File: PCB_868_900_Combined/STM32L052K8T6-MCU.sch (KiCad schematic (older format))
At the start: 27 parts, among them J2 20021121-00010C4LF, J3 B4B-PH-K-S(LF)(SN), J5 0475890001-MicroUSBPort, P1 CONN_02X03, SW2 B3U-1000P, U3 STM32L052C8T6, X3 ABM10-166-12.000MHZ-T3

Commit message: Change and Progress
connecotrs change to SMA, implemented combined PA/LNA match, currently
working on that version as primary. PCB components are placed and board
size is almost set.
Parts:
- removed J3: B4B-PH-K-S(LF)(SN), PCB_Footprints:B4B-PH-K-S(LF)(SN), symbol B4B-PH-K-S(LF)(SN)
- removed P1: CONN_02X03, Pin_Headers:Pin_Header_Straight_2x03, symbol CONN_02X03
- added J3, J4: SM06B-SRSS-TB(LF)(SN), PCB_Footprints:SM06B-SRSS-TB(LF)(SN), symbol SM06B-SRSS-TB(LF)(SN)
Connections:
- wire segments 74 -> 93

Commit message: RF Shield and more progress
Adding an RF shield to the combined implementation of the 915MHZ version
of S1G. Also experimenting with differnt connectors and what not.
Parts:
- removed J3, J4: SM06B-SRSS-TB(LF)(SN), PCB_Footprints:SM06B-SRSS-TB(LF)(SN), symbol SM06B-SRSS-TB(LF)(SN)
- added P1: CONN_02X08, Pin_Headers:Pin_Header_Straight_2x08, symbol CONN_02X08
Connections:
- net labels added: PSU_IN, VIN
- wire segments 93 -> 76

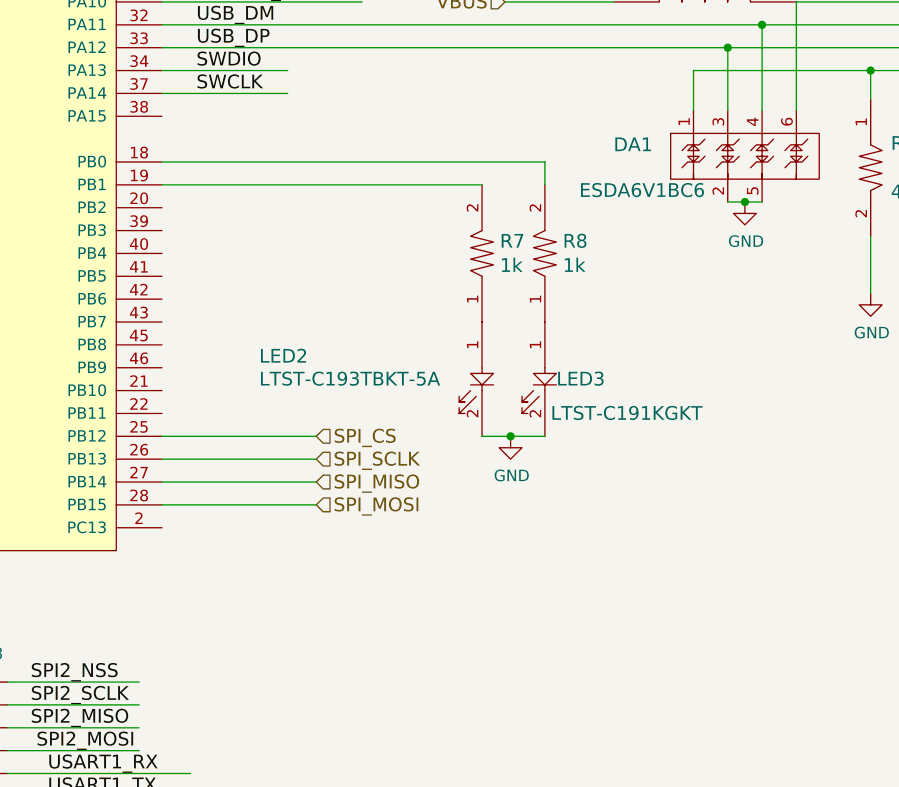
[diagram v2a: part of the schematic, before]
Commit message: First pass on PCB
First pass on PCB completed. PCB_868_900_Combined is the folder for the
finished rev.
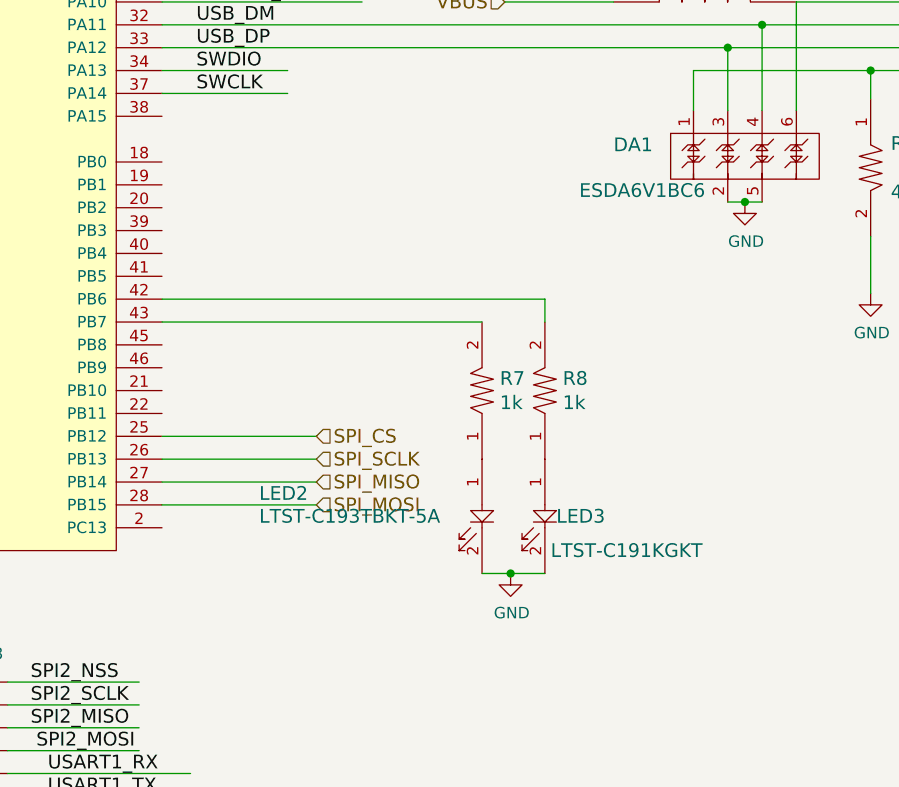
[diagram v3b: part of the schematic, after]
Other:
- moved on the sheet: LED2, LED3, R7, R8

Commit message: PCBs Tweaked A lot
PCBs have been tweaked. The separate implementation has been finished
but also has GPIOs from the MCU broken out to the connector, same for
the combined implementation. Both boards now have power indication LEDs
(red).
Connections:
- net labels added: GPIO_PA8, GPIO_PB0, GPIO_PB1, GPIO_PB10, GPIO_PB11, GPIO_PB2
- wire segments 76 -> 88
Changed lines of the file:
@@
 F 3 "" H 5575 5625 50  0000 C CNN
 	1    5575 6825
-	1    0    0    -1
+	-1   0    0    1
 $EndComp
 Text Label 6000 6975 0    60   ~ 0
 USART1_TX
-Text Label 6000 6875 0    60   ~ 0
+Text Label 4825 6975 0    60   ~ 0
 USART1_RX
 Wire Wire Line
 	5825 6975 6625 6975
 Wire Wire Line
-	5825 6875 6625 6875
-Text Label 5950 6775 0    60   ~ 0
+	4525 6975 5325 6975
+Text Label 4825 6575 0    60   ~ 0
 SPI2_MOSI
-Text Label 5925 6675 0    60   ~ 0
+Text Label 5925 6575 0    60   ~ 0
 SPI2_MISO
-Text Label 5925 6575 0    60   ~ 0
+Text Label 4825 6475 0    60   ~ 0
 SPI2_SCLK
 Text Label 5925 6475 0    60   ~ 0
 SPI2_NSS
 Wire Wire Line
-	6400 6775 5825 6775
+	5325 6575 4750 6575
 Wire Wire Line
-	5825 6575 6400 6575
+	4750 6475 5325 6475
 Wire Wire Line
 	5825 6475 6400 6475
 Wire Wire Line
-	5825 6675 6400 6675
+	5825 6575 6400 6575
 Text HLabel 10975 5250 2    60   Input ~ 0
 VIN
@@
 Text Label 10300 5250 0    60   ~ 0
 PSU_IN
-Text Label 5950 7075 0    60   ~ 0
+Text Label 4875 7175 0    60   ~ 0
 PSU_IN
 Wire Wire Line
-	6400 7075 5825 7075
+	5325 7175 4750 7175
 $Comp
 L GND #PWR42
@@
 L GND #PWR41
 U 1 1 5824B1D0
-P 5325 7175
-F 0 "#PWR41" H 5325 6925 50  0001 C CNN
-F 1 "GND" H 5330 7002 50  0000 C CNN
-F 2 "" H 5325 7175 50  0000 C CNN
-F 3 "" H 5325 7175 50  0000 C CNN
-	1    5325 7175
+P 4350 7175
+F 0 "#PWR41" H 4350 6925 50  0001 C CNN
+F 1 "GND" H 4355 7002 50  0000 C CNN
+F 2 "" H 4350 7175 50  0000 C CNN
+F 3 "" H 4350 7175 50  0000 C CNN
+	1    4350 7175
 	1    0    0    -1
 $EndComp
+Text Label 6500 4200 0    60   ~ 0
+GPIO_PB0
+Text Label 6500 4300 0    60   ~ 0
+GPIO_PB1
+Text Label 6500 4400 0    60   ~ 0
+GPIO_PB2
+Text Label 6500 5200 0    60   ~ 0
+GPIO_PB10
+Text Label 6500 5300 0    60   ~ 0
+GPIO_PB11
+Text Label 6675 3300 0    60   ~ 0
+GPIO_PA8
+Wire Wire Line
+	7225 3300 6500 3300
+Wire Wire Line
+	7050 4200 6500 4200
+Wire Wire Line
+	7050 4300 6500 4300
+Wire Wire Line
+	7050 4400 6500 4400
+Wire Wire Line
+	7050 5200 6500 5200
+Wire Wire Line
+	7050 5300 6500 5300
+Text Label 5925 6675 0    60   ~ 0
+GPIO_PB0
+Text Label 4825 6675 0    60   ~ 0
+GPIO_PB1
+Text Label 5825 6775 0    60   ~ 0
+GPIO_PB2
+Wire Wire Line
+	6375 6675 5825 6675
+Wire Wire Line
+	5325 6675 4775 6675
+Wire Wire Line
+	6375 6775 5825 6775
+Text Label 4825 6775 0    60   ~ 0
+GPIO_PB10
+Text Label 5825 6875 0    60   ~ 0
+GPIO_PB11
+Wire Wire Line
+	5325 6775 4775 6775
+Wire Wire Line
+	6375 6875 5825 6875
+Text Label 4825 6875 0    60   ~ 0
+GPIO_PA8
+Wire Wire Line
+	5325 6875 4600 6875
 $EndSCHEMATC

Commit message: Additional GPIO
Two additional GPIO pins from the STM32L0 have been added to the
connector, now there is a signal on every pin. The connector component
has been replaced with one that has a STEP 3D model for proper 3D model
exporting from KiCAD for enclosure design. This has been done to both
versions of the radio.
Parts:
- removed P1: CONN_02X08, Pin_Headers:Pin_Header_Straight_2x08, symbol CONN_02X08
- added P1: 61301621121, PCB_Footprints:61301621121, symbol 61301621121
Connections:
- net labels added: GPIO_PA15, GPIO_PB3
- wire segments 88 -> 92
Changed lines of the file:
@@
 $EndComp
 $Comp
-L GND #PWR31
+L GND #PWR030
 U 1 1 582190B8
 P 1400 5050
-F 0 "#PWR31" H 1400 4800 50  0001 C CNN
+F 0 "#PWR030" H 1400 4800 50  0001 C CNN
 F 1 "GND" H 1405 4877 50  0000 C CNN
 F 2 "" H 1400 5050 50  0000 C CNN
@@
 $EndComp
 $Comp
-L GND #PWR42
+L GND #PWR031
 U 1 1 58219186
 P 4750 5800
-F 0 "#PWR42" H 4750 5550 50  0001 C CNN
+F 0 "#PWR031" H 4750 5550 50  0001 C CNN
 F 1 "GND" H 4755 5627 50  0000 C CNN
 F 2 "" H 4750 5800 50  0000 C CNN
@@
 $EndComp
 $Comp
-L +3.3V #PWR30
+L +3.3V #PWR032
 U 1 1 58219330
 P 1400 4000
-F 0 "#PWR30" H 1400 3850 50  0001 C CNN
+F 0 "#PWR032" H 1400 3850 50  0001 C CNN
 F 1 "+3.3V" H 1415 4173 50  0000 C CNN
 F 2 "" H 1400 4000 50  0000 C CNN
@@
 $EndComp
 $Comp
-L GND #PWR39
+L GND #PWR033
 U 1 1 58219BE3
 P 3450 2950
-F 0 "#PWR39" H 3450 2700 50  0001 C CNN
+F 0 "#PWR033" H 3450 2700 50  0001 C CNN
 F 1 "GND" H 3455 2777 50  0000 C CNN
 F 2 "" H 3450 2950 50  0000 C CNN
@@
 $EndComp
 $Comp
-L +3.3V #PWR37
+L +3.3V #PWR034
 U 1 1 58219CF5
 P 3100 2500
-F 0 "#PWR37" H 3100 2350 50  0001 C CNN
+F 0 "#PWR034" H 3100 2350 50  0001 C CNN
 F 1 "+3.3V" H 3115 2673 50  0000 C CNN
 F 2 "" H 3100 2500 50  0000 C CNN
@@
 $EndComp
 $Comp
-L GND #PWR35
+L GND #PWR035
 U 1 1 5821A196
 P 1700 2950
-F 0 "#PWR35" H 1700 2700 50  0001 C CNN
+F 0 "#PWR035" H 1700 2700 50  0001 C CNN
 F 1 "GND" H 1705 2777 50  0000 C CNN
 F 2 "" H 1700 2950 50  0000 C CNN
@@
 $EndComp
 $Comp
-L GND #PWR36
+L GND #PWR036
 U 1 1 5821A1E0
 P 2500 2950
-F 0 "#PWR36" H 2500 2700 50  0001 C CNN
+F 0 "#PWR036" H 2500 2700 50  0001 C CNN
 F 1 "GND" H 2505 2777 50  0000 C CNN
 F 2 "" H 2500 2950 50  0000 C CNN
@@
 $EndComp
 $Comp
-L +3.3V #PWR34
+L +3.3V #PWR037
 U 1 1 5821A692
 P 1500 2500
-F 0 "#PWR34" H 1500 2350 50  0001 C CNN
+F 0 "#PWR037" H 1500 2350 50  0001 C CNN
 F 1 "+3.3V" H 1515 2673 50  0000 C CNN
 F 2 "" H 1500 2500 50  0000 C CNN
@@
 $EndComp
 $Comp
-L GND #PWR47
+L GND #PWR038
 U 1 1 58221381
 P 9975 3900
-F 0 "#PWR47" H 9975 3650 50  0001 C CNN
+F 0 "#PWR038" H 9975 3650 50  0001 C CNN
 F 1 "GND" H 9980 3727 50  0000 C CNN
 F 2 "" H 9975 3900 50  0000 C CNN
@@
 $EndComp
 $Comp
-L GND #PWR49
+L GND #PWR039
 U 1 1 58221B76
 P 10475 4775
-F 0 "#PWR49" H 10475 4525 50  0001 C CNN
+F 0 "#PWR039" H 10475 4525 50  0001 C CNN
 F 1 "GND" H 10480 4602 50  0000 C CNN
 F 2 "" H 10475 4775 50  0000 C CNN
@@
 $EndComp
 $Comp
-L GND #PWR46
+L GND #PWR040
 U 1 1 58223B2D
 P 9600 4775
-F 0 "#PWR46" H 9600 4525 50  0001 C CNN
+F 0 "#PWR040" H 9600 4525 50  0001 C CNN
 F 1 "GND" H 9605 4602 50  0000 C CNN
 F 2 "" H 9600 4775 50  0000 C CNN
@@
 $EndComp
 $Comp
-L GND #PWR45
+L GND #PWR041
 U 1 1 58224185
 P 9050 4375
-F 0 "#PWR45" H 9050 4125 50  0001 C CNN
+F 0 "#PWR041" H 9050 4125 50  0001 C CNN
 F 1 "GND" H 9055 4202 50  0000 C CNN
 F 2 "" H 9050 4375 50  0000 C CNN
@@
 $EndComp
 $Comp
-L GND #PWR48
+L GND #PWR042
 U 1 1 58224D2B
 P 10425 3125
-F 0 "#PWR48" H 10425 2875 50  0001 C CNN
+F 0 "#PWR042" H 10425 2875 50  0001 C CNN
 F 1 "GND" H 10430 2952 50  0000 C CNN
 F 2 "" H 10425 3125 50  0000 C CNN
@@
 NRST
 $Comp
-L GND #PWR33
+L GND #PWR043
 U 1 1 5824BA14
 P 1400 6250
-F 0 "#PWR33" H 1400 6000 50  0001 C CNN
+F 0 "#PWR043" H 1400 6000 50  0001 C CNN
 F 1 "GND" H 1405 6077 50  0000 C CNN
 F 2 "" H 1400 6250 50  0000 C CNN
@@
 $EndComp
 $Comp
-L +3.3V #PWR32
+L +3.3V #PWR044
 U 1 1 5824BBC1
 P 1400 5575
-F 0 "#PWR32" H 1400 5425 50  0001 C CNN
+F 0 "#PWR044" H 1400 5425 50  0001 C CNN
 F 1 "+3.3V" H 1415 5748 50  0000 C CNN
 F 2 "" H 1400 5575 50  0000 C CNN
@@
 $EndComp
 $Comp
-L GND #PWR44
+L GND #PWR045
 U 1 1 58250111
 P 8025 6000
-F 0 "#PWR44" H 8025 5750 50  0001 C CNN
+F 0 "#PWR045" H 8025 5750 50  0001 C CNN
 F 1 "GND" H 8030 5827 50  0000 C CNN
 F 2 "" H 8025 6000 50  0000 C CNN
@@
 $EndComp
 $Comp
-L GND #PWR40
+L GND #PWR046
 U 1 1 582650D6
 P 4150 4375
-F 0 "#PWR40" H 4150 4125 50  0001 C CNN
+F 0 "#PWR046" H 4150 4125 50  0001 C CNN
 F 1 "GND" H 4155 4202 50  0000 C CNN
 F 2 "" H 4150 4375 50  0000 C CNN
@@
 Connection ~ 3250 4200
 $Comp
-L GND #PWR38
+L GND #PWR047
 U 1 1 58299A73
 P 3125 4200
-F 0 "#PWR38" H 3125 3950 50  0001 C CNN
+F 0 "#PWR047" H 3125 3950 50  0001 C CNN
 F 1 "GND" H 3130 4027 50  0000 C CNN
 F 2 "" H 3125 4200 50  0000 C CNN
@@
 $EndComp
 Connection ~ 3125 4200
-$Comp
-L CONN_02X08 P1
-U 1 1 5823F6D4
-P 5575 6825
-F 0 "P1" H 5575 7390 50  0000 C CNN
-F 1 "CONN_02X08" H 5575 7299 50  0000 C CNN
-F 2 "Pin_Headers:Pin_Header_Straight_2x08" H 5575 5625 50  0001 C CNN
-F 3 "" H 5575 5625 50  0000 C CNN
-	1    5575 6825
-	-1   0    0    1
-$EndComp
-Text Label 6000 6975 0    60   ~ 0
+Text Label 6100 6975 0    60   ~ 0
 USART1_TX
 Text Label 4825 6975 0    60   ~ 0
 USART1_RX
 Wire Wire Line
-	5825 6975 6625 6975
+	5925 6975 6725 6975
 Wire Wire Line
 	4525 6975 5325 6975
 Text Label 4825 6575 0    60   ~ 0
 SPI2_MOSI
-Text Label 5925 6575 0    60   ~ 0
+Text Label 6025 6575 0    60   ~ 0
 SPI2_MISO
 Text Label 4825 6475 0    60   ~ 0
 SPI2_SCLK
-Text Label 5925 6475 0    60   ~ 0
+Text Label 6025 6475 0    60   ~ 0
 SPI2_NSS
 Wire Wire Line
@@
 	4750 6475 5325 6475
 Wire Wire Line
-	5825 6475 6400 6475
-Wire Wire Line
-	5825 6575 6400 6575
+	5925 6475 6500 6475
+Wire Wire Line
+	5925 6575 6500 6575
 Text HLabel 10975 5250 2    60   Input ~ 0
 VIN
@@
 	5325 7175 4750 7175
 $Comp
-L GND #PWR43
+L GND #PWR048
 U 1 1 58246BF1
-P 5825 7175
-F 0 "#PWR43" H 5825 6925 50  0001 C CNN
-F 1 "GND" H 5830 7002 50  0000 C CNN
-F 2 "" H 5825 7175 50  0000 C CNN
-F 3 "" H 5825 7175 50  0000 C CNN
-	1    5825 7175
-	1    0    0    -1
-$EndComp
-$Comp
-L GND #PWR41
+P 5925 7175
+F 0 "#PWR048" H 5925 6925 50  0001 C CNN
+F 1 "GND" H 5930 7002 50  0000 C CNN
+F 2 "" H 5925 7175 50  0000 C CNN
+F 3 "" H 5925 7175 50  0000 C CNN
+	1    5925 7175
+	1    0    0    -1
+$EndComp
+$Comp
+L GND #PWR049
 U 1 1 5824B1D0
 P 4350 7175
-F 0 "#PWR41" H 4350 6925 50  0001 C CNN
+F 0 "#PWR049" H 4350 6925 50  0001 C CNN
 F 1 "GND" H 4355 7002 50  0000 C CNN
 F 2 "" H 4350 7175 50  0000 C CNN
@@
 Wire Wire Line
 	7050 5300 6500 5300
-Text Label 5925 6675 0    60   ~ 0
+Text Label 6025 6675 0    60   ~ 0
 GPIO_PB0
 Text Label 4825 6675 0    60   ~ 0
 GPIO_PB1
-Text Label 5825 6775 0    60   ~ 0
+Text Label 5925 6775 0    60   ~ 0
 GPIO_PB2
 Wire Wire Line
-	6375 6675 5825 6675
+	6475 6675 5925 6675
 Wire Wire Line
 	5325 6675 4775 6675
 Wire Wire Line
-	6375 6775 5825 6775
+	6475 6775 5925 6775
 Text Label 4825 6775 0    60   ~ 0
 GPIO_PB10
-Text Label 5825 6875 0    60   ~ 0
+Text Label 5925 6875 0    60   ~ 0
 GPIO_PB11
 Wire Wire Line
 	5325 6775 4775 6775
 Wire Wire Line
-	6375 6875 5825 6875
+	6475 6875 5925 6875
 Text Label 4825 6875 0    60   ~ 0
 GPIO_PA8
 Wire Wire Line
 	5325 6875 4600 6875
+$Comp
+L 61301621121 P1
+U 1 1 582B3533
+P 5525 7075
+F 0 "P1" H 5425 6238 60  0000 C CNN
+F 1 "61301621121" H 5425 6344 60  0000 C CNN
+F 2 "PCB_Footprints:61301621121" H 5675 7375 60  0001 C CNN
+F 3 "http://katalog.we-online.de/em/datasheet/6130xx21121.pdf" H 5250 7450 60  0001 C CNN
+F 4 "0.71280 @ 500" H 5350 7550 60  0001 C CNN "Cost"
+F 5 "14 Nov 2016" H 5450 7650 60  0001 C CNN "Date Created "
+F 6 "14 Nov 2016" H 5550 7750 60  0001 C CNN "Date Modified"
+F 7 "Adam Vadala-Roth" H 5650 7850 60  0001 C CNN "Designer "
+F 8 "8.54mm" H 5750 7950 60  0001 C CNN "Height"
+F 9 "Yes" H 5850 8050 60  0001 C CNN "RHoS?"
+F 10 "Wurth Electronics Inc" H 5950 8150 60  0001 C CNN "MFR"
+F 11 "B3B-PH-SM4-TB(LF)(SN)" H 6050 8250 60  0001 C CNN "MFR#"
+F 12 "SMT/SMD" H 6150 8350 60  0001 C CNN "Mounting"
+F 13 "16" H 6250 8450 60  0001 C CNN "Pin Count#"
+F 14 "Active" H 6350 8550 60  0001 C CNN "Status"
+F 15 "N/A" H 6450 8650 60  0001 C CNN "Tolerance"
+F 16 "Throughhole Pin Header 2.54mm Pitch" H 6550 8750 60  0001 C CNN "Type"
+F 17 "N/A" H 6650 8850 60  0001 C CNN "Voltage"
+F 18 "N/A" H 6750 8950 60  0001 C CNN "Wattage"
+F 19 "N/A" H 6850 9050 60  0001 C CNN "Component-Value"
+F 20 "16 Positions Header, Unshrouded Connector 0.100\" (2.54mm) Through Hole Gold" H 6950 9150 60  0001 C CNN "Description"
+	1    5525 7075
+	-1   0    0    1
+$EndComp
+Text Label 6500 4500 0    60   ~ 0
+GPIO_PB3
+Text Label 6500 4000 0    60   ~ 0
+GPIO_PA15
+Wire Wire Line
+	7050 4000 6500 4000
+Wire Wire Line
+	7050 4500 6500 4500
+Text Label 4850 7075 0    60   ~ 0
+GPIO_PB3
+Text Label 5925 7075 0    60   ~ 0
+GPIO_PA15
+Wire Wire Line
+	4525 7075 5325 7075
+Wire Wire Line
+	5925 7075 6725 7075
 $EndSCHEMATC
